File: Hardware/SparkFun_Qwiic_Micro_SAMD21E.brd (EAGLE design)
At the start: 25.4 x 25.4 mm, 77 parts, among them Q1 3.1A/30V/105mΩ, U1 3.3V, U2 W25Q32FV, U3 SAMD21E

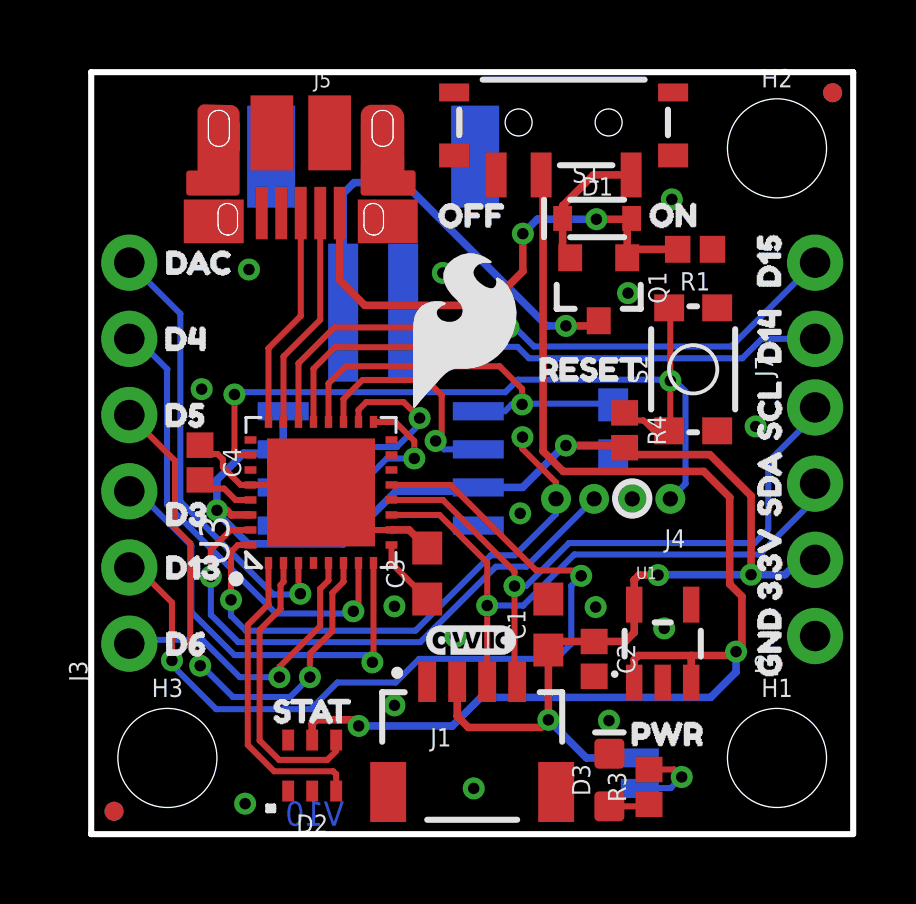
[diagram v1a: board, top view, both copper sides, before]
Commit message: Attaches analog voltage pin to 3.3V power rail
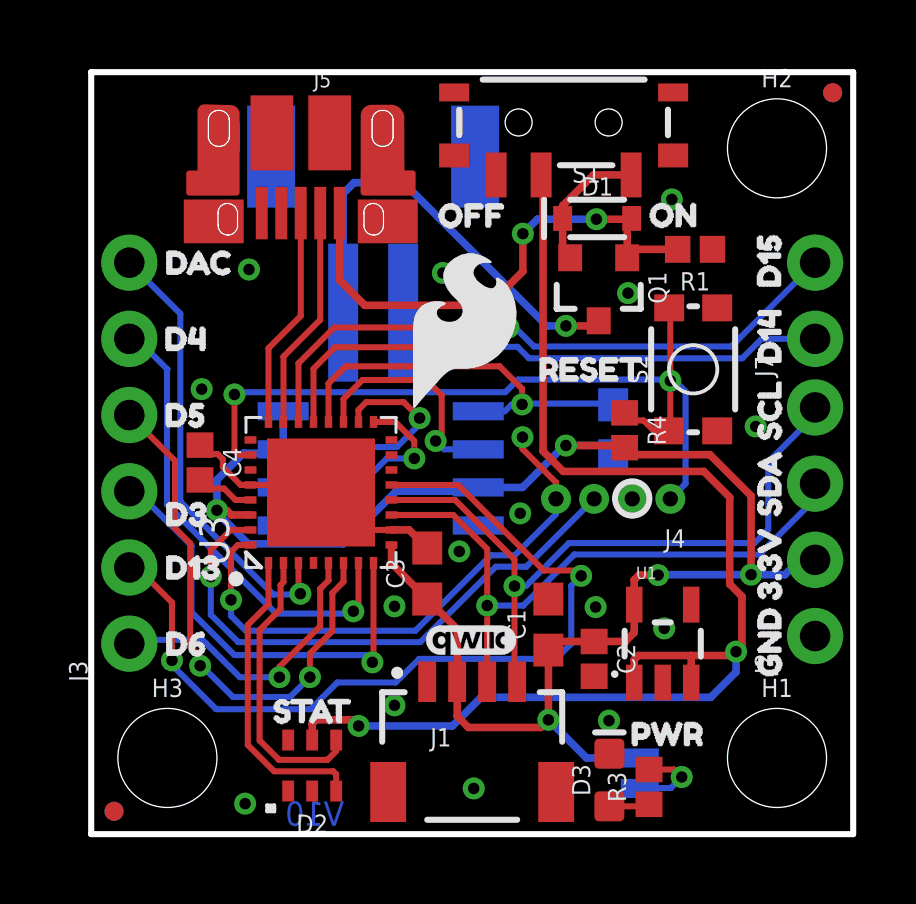
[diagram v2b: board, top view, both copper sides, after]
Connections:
- removed net VDDA: C3.1, U3.VDD
- net 3.3V: now also C3.1, U3.VDD
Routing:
- net 3.3V: track 52.3 -> 58.7 mm
- net VDDA: track 2.30 -> 0.00 mm
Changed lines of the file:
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@@
 <setting verticaltext="up"/>
 </settings>
-<grid distance="0.05" unitdist="inch" unit="inch" style="lines" multiple="1" display="yes" altdistance="0.001" altunitdist="inch" altunit="inch"/>
+<grid distance="0.01" unitdist="inch" unit="inch" style="lines" multiple="1" display="yes" altdistance="0.001" altunitdist="inch" altunit="inch"/>
 <layers>
 <layer number="1" name="Top" color="4" fill="1" visible="yes" active="yes"/>
@@
 <layer number="115" name="ReferenceISLANDS" color="7" fill="1" visible="no" active="no"/>
 <layer number="116" name="Patch_BOT" color="9" fill="4" visible="no" active="no"/>
-<layer number="117" name="PM_Ref" color="26" fill="1" visible="no" active="yes"/>
+<layer number="117" name="PM_Ref" color="26" fill="1" visible="yes" active="yes"/>
 <layer number="118" name="Rect_Pads" color="7" fill="1" visible="no" active="no"/>
-<layer number="119" name="PF_Ref" color="31" fill="1" visible="no" active="yes"/>
-<layer number="120" name="WFL_Ref" color="25" fill="1" visible="no" active="yes"/>
+<layer number="119" name="PF_Ref" color="31" fill="1" visible="yes" active="yes"/>
+<layer number="120" name="WFL_Ref" color="25" fill="1" visible="yes" active="yes"/>
 <layer number="121" name="_tsilk" color="7" fill="1" visible="no" active="no"/>
 <layer number="122" name="_bsilk" color="7" fill="1" visible="no" active="no"/>
@@
 <via x="3.683" y="14.8336" extent="1-16" drill="0.381"/>
 <via x="17.8943" y="18.034" extent="1-16" drill="0.381"/>
-<via x="12.1412" y="6.5786" extent="1-16" drill="0.381"/>
 <via x="10.1092" y="4.2926" extent="1-16" drill="0.381"/>
 <contactref element="J6" pad="1"/>
+<via x="12.2682" y="9.4234" extent="1-16" drill="0.381"/>
 </signal>
 <signal name="DAC">
@@
 <wire x1="24.13" y1="13.97" x2="24.13" y2="14.224" width="0.2032" layer="16"/>
 <contactref element="U3" pad="PA09"/>
-<wire x1="11.72" y1="11.14" x2="10.01" y2="11.14" width="0.2032" layer="1"/>
+<wire x1="12.1264" y1="11.14" x2="10.01" y2="11.14" width="0.2032" layer="1"/>
 <wire x1="14.1097" y1="5.1703" x2="14.1097" y2="8.2677" width="0.2032" layer="1"/>
-<wire x1="14.1097" y1="8.2677" x2="14.1097" y2="8.7503" width="0.2032" layer="1"/>
+<wire x1="14.1097" y1="8.2677" x2="14.1097" y2="9.1567" width="0.2032" layer="1"/>
 <wire x1="14.1097" y1="8.2677" x2="14.4907" y2="8.2677" width="0.2032" layer="16"/>
 <wire x1="14.4907" y1="8.2677" x2="15.9258" y2="9.7028" width="0.2032" layer="16"/>
-<wire x1="14.1097" y1="8.7503" x2="11.72" y2="11.14" width="0.2032" layer="1"/>
+<wire x1="14.1097" y1="9.1567" x2="12.1264" y2="11.14" width="0.2032" layer="1"/>
 <wire x1="14.2" y1="5.08" x2="14.1097" y2="5.1703" width="0.2032" layer="1"/>
 </signal>
 <signal name="SDA">
 <contactref element="J1" pad="3"/>
-<wire x1="13.2" y1="9.0504" x2="13.2" y2="7.62" width="0.2032" layer="1"/>
+<wire x1="13.2" y1="9.5076" x2="13.2" y2="7.62" width="0.2032" layer="1"/>
 <via x="13.2" y="7.62" extent="1-16" drill="0.381"/>
 <wire x1="14.4018" y1="7.62" x2="13.2" y2="7.62" width="0.2032" layer="16"/>
 <wire x1="24.13" y1="11.176" x2="22.2758" y2="9.3218" width="0.2032" layer="16"/>
-<wire x1="13.2" y1="9.0504" x2="11.6104" y2="10.64" width="0.2032" layer="1"/>
+<wire x1="13.2" y1="9.5076" x2="12.0676" y2="10.64" width="0.2032" layer="1"/>
 <wire x1="22.2758" y1="9.3218" x2="16.1036" y2="9.3218" width="0.2032" layer="16"/>
 <wire x1="16.1036" y1="9.3218" x2="14.4018" y2="7.62" width="0.2032" layer="16"/>
@@
 <wire x1="13.2" y1="5.08" x2="13.2" y2="7.62" width="0.2032" layer="1"/>
 <contactref element="U3" pad="PA08"/>
-<wire x1="11.6104" y1="10.64" x2="10.01" y2="10.64" width="0.2032" layer="1"/>
+<wire x1="12.0676" y1="10.64" x2="10.01" y2="10.64" width="0.2032" layer="1"/>
 </signal>
 <signal name="RX">
@@
 <wire x1="20.6248" y1="12.6492" x2="18.0128" y2="12.6492" width="0.254" layer="1"/>
 <wire x1="18.0128" y1="12.6492" x2="17.78" y2="12.882" width="0.254" layer="1"/>
+<contactref element="U3" pad="VDD"/>
+<contactref element="C3" pad="1"/>
+<wire x1="12.2" y1="5.08" x2="12.2" y2="5.5678875" width="0.254" layer="1"/>
+<wire x1="11.4681" y1="7.5701" x2="11.2014" y2="7.8368" width="0.254" layer="1"/>
+<wire x1="10.01" y1="9.64" x2="10.01" y2="9.0282" width="0.254" layer="1"/>
+<wire x1="10.01" y1="9.0282" x2="11.1701" y2="7.8681" width="0.254" layer="1"/>
+<wire x1="11.1701" y1="7.8681" x2="11.2014" y2="7.8368" width="0.254" layer="1"/>
+<wire x1="12.2" y1="5.08" x2="12.2" y2="6.8382" width="0.254" layer="1"/>
+<wire x1="12.2" y1="6.8382" x2="11.2014" y2="7.8368" width="0.254" layer="1"/>
 </signal>
 <signal name="MOSI">
@@
 <wire x1="15.494" y1="5.842" x2="16.002" y2="6.35" width="0.2032" layer="16"/>
 <wire x1="2.6924" y1="7.7216" x2="2.6924" y2="5.7912" width="0.2032" layer="1"/>
-<wire x1="16.1544" y1="8.7884" x2="14.8336" y2="8.7884" width="0.2032" layer="1"/>
+<wire x1="16.1544" y1="8.7884" x2="15.0876" y2="8.7884" width="0.2032" layer="1"/>
 <wire x1="16.1544" y1="8.7884" x2="16.3322" y2="8.6106" width="0.2032" layer="1"/>
 <wire x1="16.002" y1="6.35" x2="16.002" y2="8.2804" width="0.2032" layer="16"/>
 <wire x1="16.002" y1="8.2804" x2="16.3322" y2="8.6106" width="0.2032" layer="16"/>
-<wire x1="14.8336" y1="8.7884" x2="11.982" y2="11.64" width="0.2032" layer="1"/>
+<wire x1="15.0876" y1="8.7884" x2="12.236" y2="11.64" width="0.2032" layer="1"/>
 <wire x1="4.1656" y1="4.1656" x2="7.3152" y2="4.1656" width="0.2032" layer="16"/>
 <wire x1="7.3152" y1="4.1656" x2="8.2042" y2="5.0546" width="0.2032" layer="16"/>
@@
 <wire x1="2.6924" y1="5.6388" x2="4.1656" y2="4.1656" width="0.2032" layer="16"/>
 <contactref element="U3" pad="PA10"/>
-<wire x1="11.982" y1="11.64" x2="10.01" y2="11.64" width="0.2032" layer="1"/>
+<wire x1="12.236" y1="11.64" x2="10.01" y2="11.64" width="0.2032" layer="1"/>
 </signal>
 <signal name="VIN1">
@@
 <wire x1="16.7407" y1="21.9736" x2="17.998" y2="21.9736" width="0.254" layer="1"/>
 </signal>
-<signal name="VDDA">
-<contactref element="C3" pad="1"/>
-<wire x1="10.01" y1="9.0282" x2="11.2014" y2="7.8368" width="0.2032" layer="1"/>
-<contactref element="U3" pad="VDD"/>
-<wire x1="10.01" y1="9.64" x2="10.01" y2="9.0282" width="0.2032" layer="1"/>
-</signal>
 <signal name="V_BATT">

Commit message: Moves silk around in various spots, rotates LED to make space for PWR silk
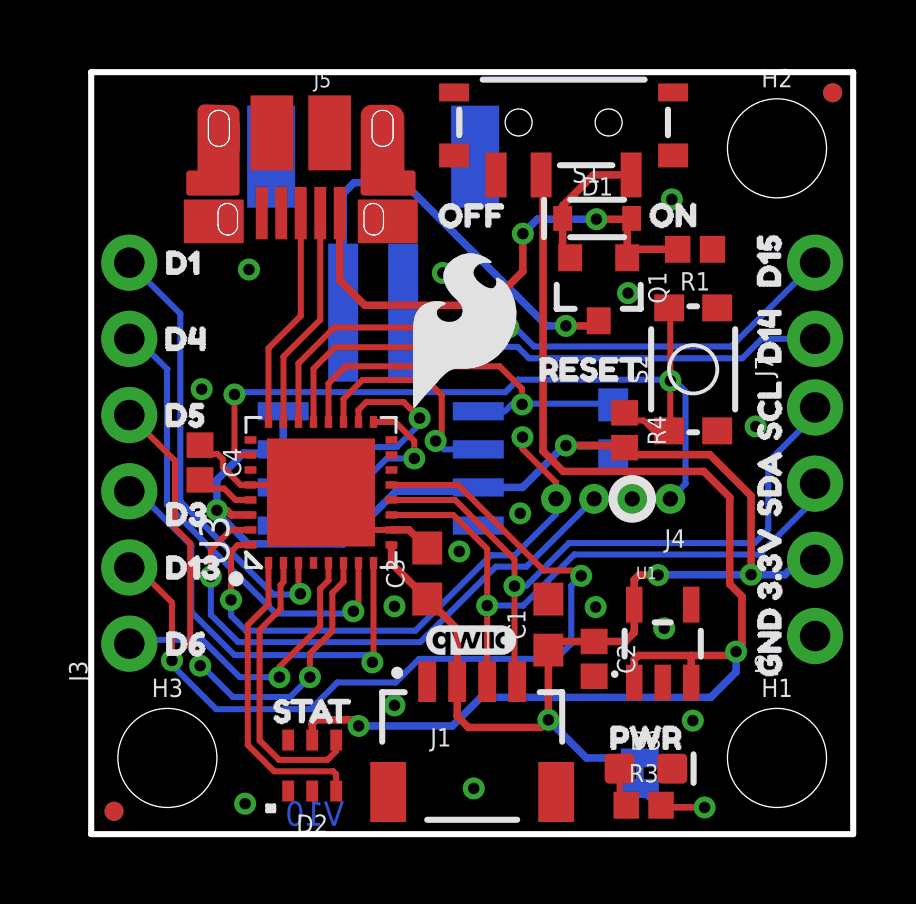
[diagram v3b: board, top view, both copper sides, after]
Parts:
- removed U$22: (no value), SamD21:SAMD211
- removed U$43: (no value), buzzard_labels:DAC0
- added U$1: (no value), D0:D00
- added U$10: (no value), D0:QWIIC2
- U$15: device MICRO:MICRO0 -> D0:SAMD213
- U$17: device BUZZARD_BOTTOM:GND0 -> Labels:3V3-03
- U$2: device BUZZARD_BOTTOM:3#3V1 -> Labels:GND-03
- U$23: device SparkFun-Aesthetics:QWIIC_6MM -> D0:MICRO2
- U$6: device Underside Labels:D0#SDA3 -> D0:D12
- moved U$6 23.0 mm to (1.78, 19.1), flipped to the top
- moved LOGO3 15.6 mm to (16.3, 18.0)
- moved U$15 3.79 mm to (15.2, 4.06)
- moved U$2 2.64 mm to (23.8, 6.50)
- moved U$17 2.49 mm to (23.8, 9.09)
- moved U$23 2.17 mm to (11.9, 5.84)
- moved U$18 1.44 mm to (19.9, 21.7)
- moved D3 1.28 mm to (18.5, 2.18), turned to 0 degrees
- moved U$19 1.05 mm to (16.8, 21.6)
- moved U$47 0.72 mm to (16.6, 3.21)
- moved R3 0.64 mm to (18.4, 0.97), turned to 0 degrees
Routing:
- net N$2: track 2.75 -> 3.92 mm

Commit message: Updates numbering on samd21E
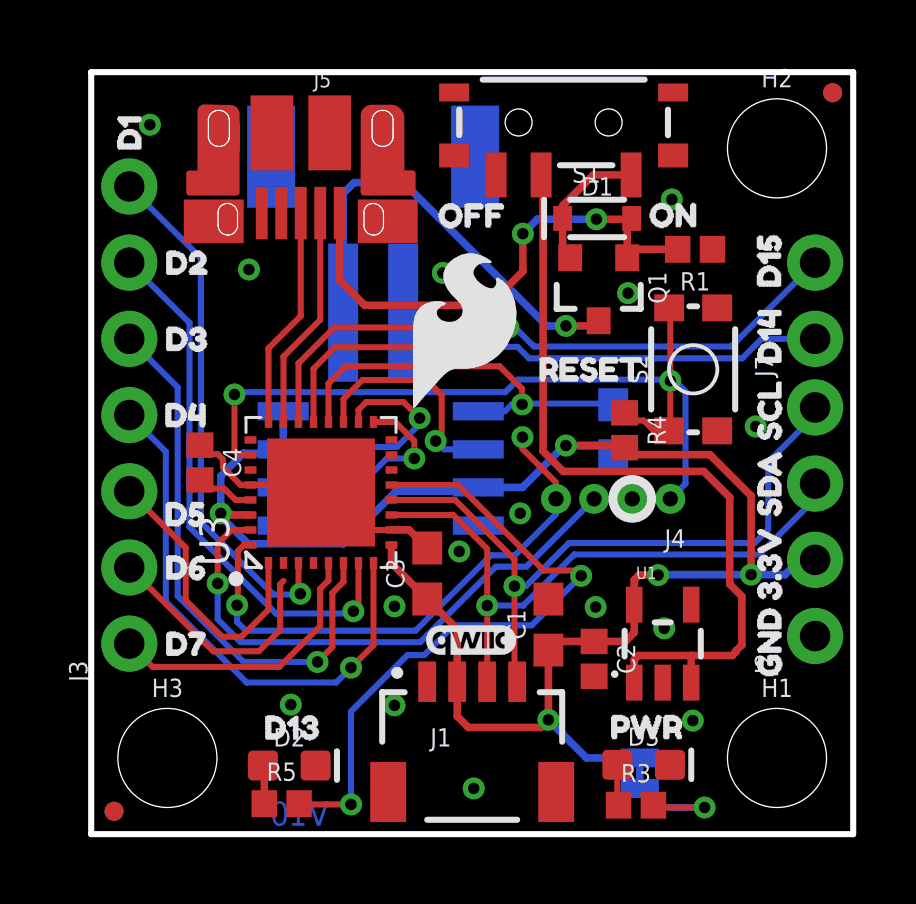
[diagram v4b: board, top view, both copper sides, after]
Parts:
- removed U$11: (no value), Underside Labels:D69
- removed U$40: (no value), buzzard_labels:D134
- removed U$51: (no value), buzzard_labels:STAT15
- removed U$7: (no value), Underside Labels:D2#SCL2
- added R5: 1K, SparkFun-Resistors:0402
- added U$27: (no value), Moar labels!:D136
- added U$28: (no value), Renumbering:D21
- D2: value APA102-2020 -> BLUE; device SparkFun-LED:APA102-2020 -> SparkFun-LED:LED-0603
- J3: device SparkFun-Connectors:1X06_NO_SILK -> SparkFun-Connectors:1X07_NO_SILK
- U$12: device Underside Labels:D138 -> Moar labels!:D75
- U$13: device Underside Labels:DAC4 -> Moar labels!:DAC1
- U$16: device Underside Labels:MOSI5 -> Moar labels!:MOSI2
- moved U$36 5.84 mm to (1.78, 16.5)
- moved U$13 5.04 mm to (1.27, 22.1), turned to 90 degrees
- moved U$12 3.95 mm to (1.78, 6.35), flipped to the top
- moved U$38 3.30 mm to (1.79, 10.7)
- moved U$6 3.09 mm to (1.27, 22.1), turned to 90 degrees
- moved U$16 2.62 mm to (5.69, 19.1)
- moved U$20 2.59 mm to (5.23, 13.9)
- moved U$37 2.54 mm to (1.78, 14.0)
- moved U$39 2.54 mm to (1.78, 8.89)
- moved U$14 2.49 mm to (5.68, 16.5)
- moved D2 0.76 mm to (6.60, 2.29), turned to 0 degrees
- moved U$47 0.36 mm to (16.6, 3.57)
- moved R3 0.25 mm to (18.2, 0.97)
- moved D3 0.15 mm to (18.4, 2.31)
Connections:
- removed net CI: D2.CKI, U3.PA01
- removed net DI: D2.SDI, U3.PA00
- new net D5: J3.3, U3.PA00
- new net D7: J3.1, U3.PA04
- new net N$4: D2.A, R5.1
- net D13: now also R5.2; no longer J3.2
- net D6: now also J3.2, U3.PA01; no longer J3.1, U3.PA04
- net DAC: now also J3.7; no longer J3.6
- net GND: now also D2.C; no longer D2.GND
- net MISO: now also J3.5; no longer J3.4
- net MOSI: now also J3.6; no longer J3.5
- net SCK: now also J3.4; no longer J3.3
- net VIN: no longer D2.VDD
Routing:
- net VIN: track 42.9 -> 26.7 mm, vias 2 -> 0
- net DI: track 10.3 -> 0.00 mm
- net D5: track 0.00 -> 9.61 mm
- net CI: track 9.56 -> 0.00 mm
- net D7: track 0.00 -> 9.47 mm
- net D13: track 28.8 -> 22.0 mm
- net SCK: track 15.1 -> 18.0 mm
- net DAC: track 15.0 -> 17.6 mm
- net MOSI: track 15.6 -> 18.0 mm
- net D6: track 10.1 -> 8.16 mm, vias 1 -> 0
- net N$4: track 0.00 -> 1.29 mm
- net 3.3V: track 58.7 -> 57.5 mm
- net MISO: track 18.0 -> 18.5 mm, vias 2 -> 1

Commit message: Huge update
* Changes pin layout in arduino files which are now reflected in SAMD21 symbol
* reroutes different lines to the headers on the left side of the board
* removes the APA102 in favor of blue stat LED
* Changes Qwiic Micro Arduino pin order and internal APA102 pin assignments
* Adds gerbers
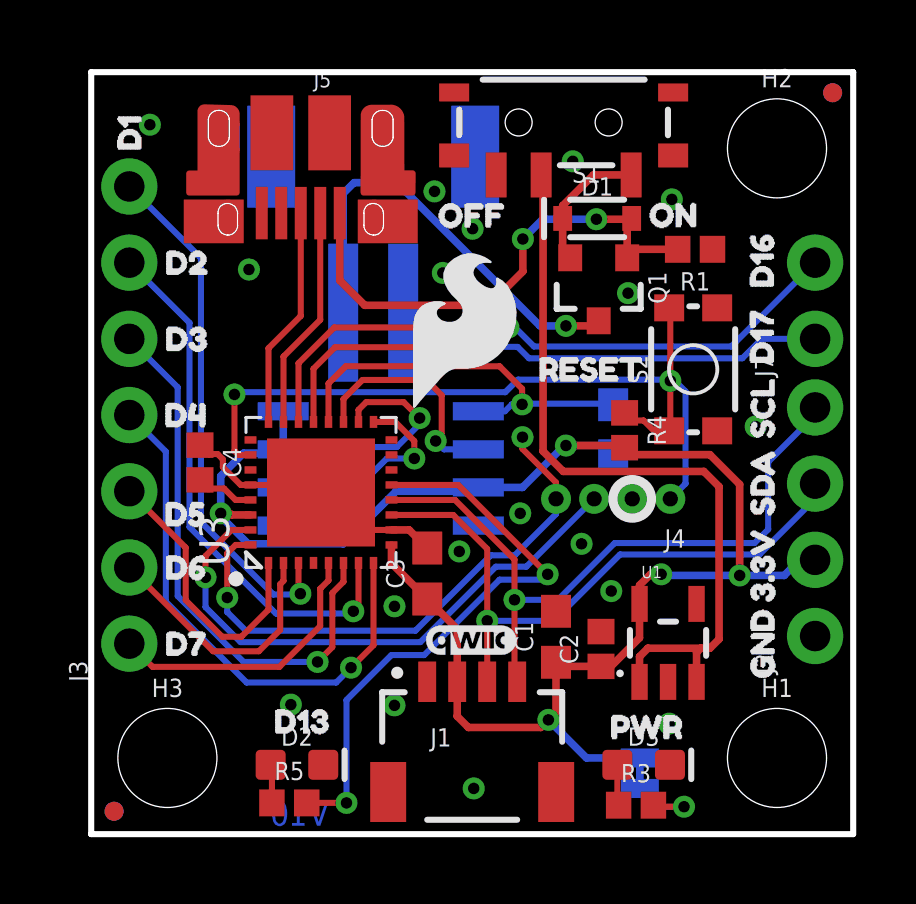
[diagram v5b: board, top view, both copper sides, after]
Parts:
- removed U$41: (no value), buzzard_labels:D147
- removed U$42: (no value), buzzard_labels:D156
- added U$11: (no value), Renumbering:D17#RX3
- added U$22: (no value), Renumbering:D85
- added U$25: (no value), Renumbering:D50
- added U$26: (no value), Renumbering:D61
- added U$29: (no value), Moar labels!:D136
- added U$7: (no value), Renumbering:D166
- U$27: device Moar labels!:D136 -> Renumbering:D72
- U$8: device Underside Labels:D14#TX1 -> Renumbering:D177
- U$9: device Underside Labels:D15#RX0 -> Renumbering:D16#TX4
- moved U$27 2.91 mm to (4.37, 6.38), flipped to the bottom
- moved U$8 2.03 mm to (22.4, 15.0), flipped to the top, turned to 90 degrees
- moved C1 0.48 mm to (15.5, 6.58)
- moved C2 0.40 mm to (17.0, 6.17), turned to 90 degrees
- moved R5 0.26 mm to (6.60, 1.04)
- moved D2 0.26 mm to (6.86, 2.31)
- moved U$49 0.24 mm to (22.4, 12.5)
- moved U$44 0.23 mm to (22.4, 4.52)
- moved U$5 0.23 mm to (22.4, 7.06)
- moved U$50 0.23 mm to (22.4, 9.93)
- moved U1 0.18 mm to (19.2, 6.38)
- moved U$9 0.06 mm to (23.7, 19.0)
- moved U$20 0.05 mm to (5.23, 14.0)
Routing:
- net D13: track 22.0 -> 19.6 mm
- net N$2: track 4.16 -> 2.77 mm
- net VIN: track 26.7 -> 25.6 mm
- net D6: track 8.16 -> 8.76 mm
- net GND: vias 15 -> 18

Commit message: New bootloader, updates samd21 with latest package
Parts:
- U3: value SAMD21E -> ATSAMD21E18A-U; device SparkFun-IC-Microcontroller:QFN32 -> SparkFun-IC-Microcontroller:QFN-32_SAMD
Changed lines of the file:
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@@
 <drawing>
 <settings>
-<setting alwaysvectorfont="yes"/>
+<setting alwaysvectorfont="no"/>
 <setting verticaltext="up"/>
 </settings>
@@
 <layer number="37" name="tTest" color="7" fill="1" visible="no" active="yes"/>
 <layer number="38" name="bTest" color="7" fill="1" visible="no" active="yes"/>
-<layer number="39" name="tKeepout" color="4" fill="11" visible="yes" active="yes"/>
+<layer number="39" name="tKeepout" color="4" fill="11" visible="no" active="yes"/>
 <layer number="40" name="bKeepout" color="1" fill="11" visible="no" active="yes"/>
 <layer number="41" name="tRestrict" color="4" fill="10" visible="no" active="yes"/>
@@
 <layer number="115" name="ReferenceISLANDS" color="7" fill="1" visible="no" active="no"/>
 <layer number="116" name="Patch_BOT" color="9" fill="4" visible="no" active="no"/>
-<layer number="117" name="PM_Ref" color="26" fill="1" visible="no" active="yes"/>
+<layer number="117" name="PM_Ref" color="26" fill="1" visible="yes" active="yes"/>
 <layer number="118" name="Rect_Pads" color="7" fill="1" visible="no" active="no"/>
-<layer number="119" name="PF_Ref" color="31" fill="1" visible="no" active="yes"/>
-<layer number="120" name="WFL_Ref" color="25" fill="1" visible="no" active="yes"/>
+<layer number="119" name="PF_Ref" color="31" fill="1" visible="yes" active="yes"/>
+<layer number="120" name="WFL_Ref" color="25" fill="1" visible="yes" active="yes"/>
 <layer number="121" name="_tsilk" color="7" fill="1" visible="no" active="no"/>
 <layer number="122" name="_bsilk" color="7" fill="1" visible="no" active="no"/>
@@
 <element name="U$50" library="buzzard_labels" package="SDA9" value="" x="22.3774" y="9.9314" smashed="yes" rot="R90"/>
 <element name="U$21" library="RESET" package="RESET0" value="" x="14.224" y="15.494" smashed="yes"/>
-<element name="U3" library="SparkFun-IC-Microcontroller" package="QFN32" value="SAMD21E" x="7.62" y="11.43" smashed="yes" rot="R90">
+<element name="U3" library="SparkFun-IC-Microcontroller" package="QFN-32_SAMD" value="ATSAMD21E18A-U" x="7.62" y="11.43" smashed="yes" rot="R90">
 <attribute name="NAME" x="4.6" y="8.94" size="1" layer="25" rot="R90"/>
 <attribute name="PROD_ID" value="IC-14428" x="7.62" y="11.43" size="1.778" layer="27" rot="R90" display="off"/>
